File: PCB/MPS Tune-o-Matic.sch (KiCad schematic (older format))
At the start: 19 parts, among them J1 ISP, J2 MPS, U1 ATmega328P, U4 BMP390, Y1 FA-238 16.0000MB-C3

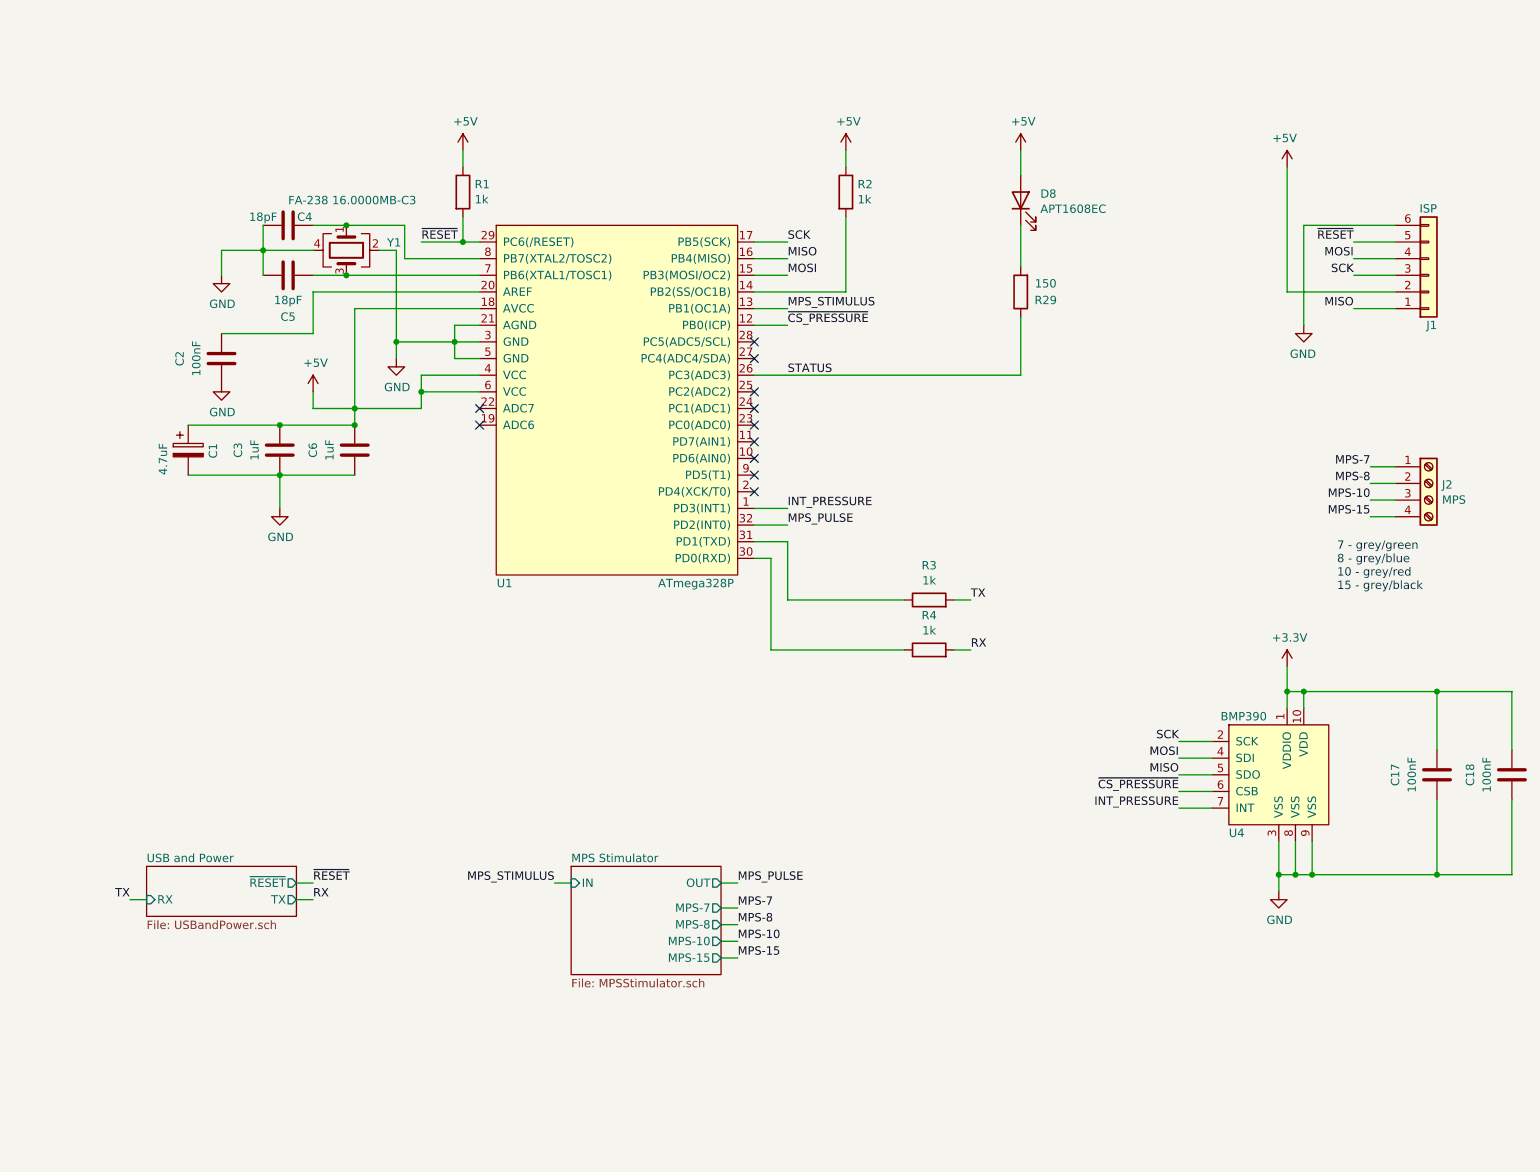
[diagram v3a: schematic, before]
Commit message: Started work on V2.0 with vacuum monitoring.
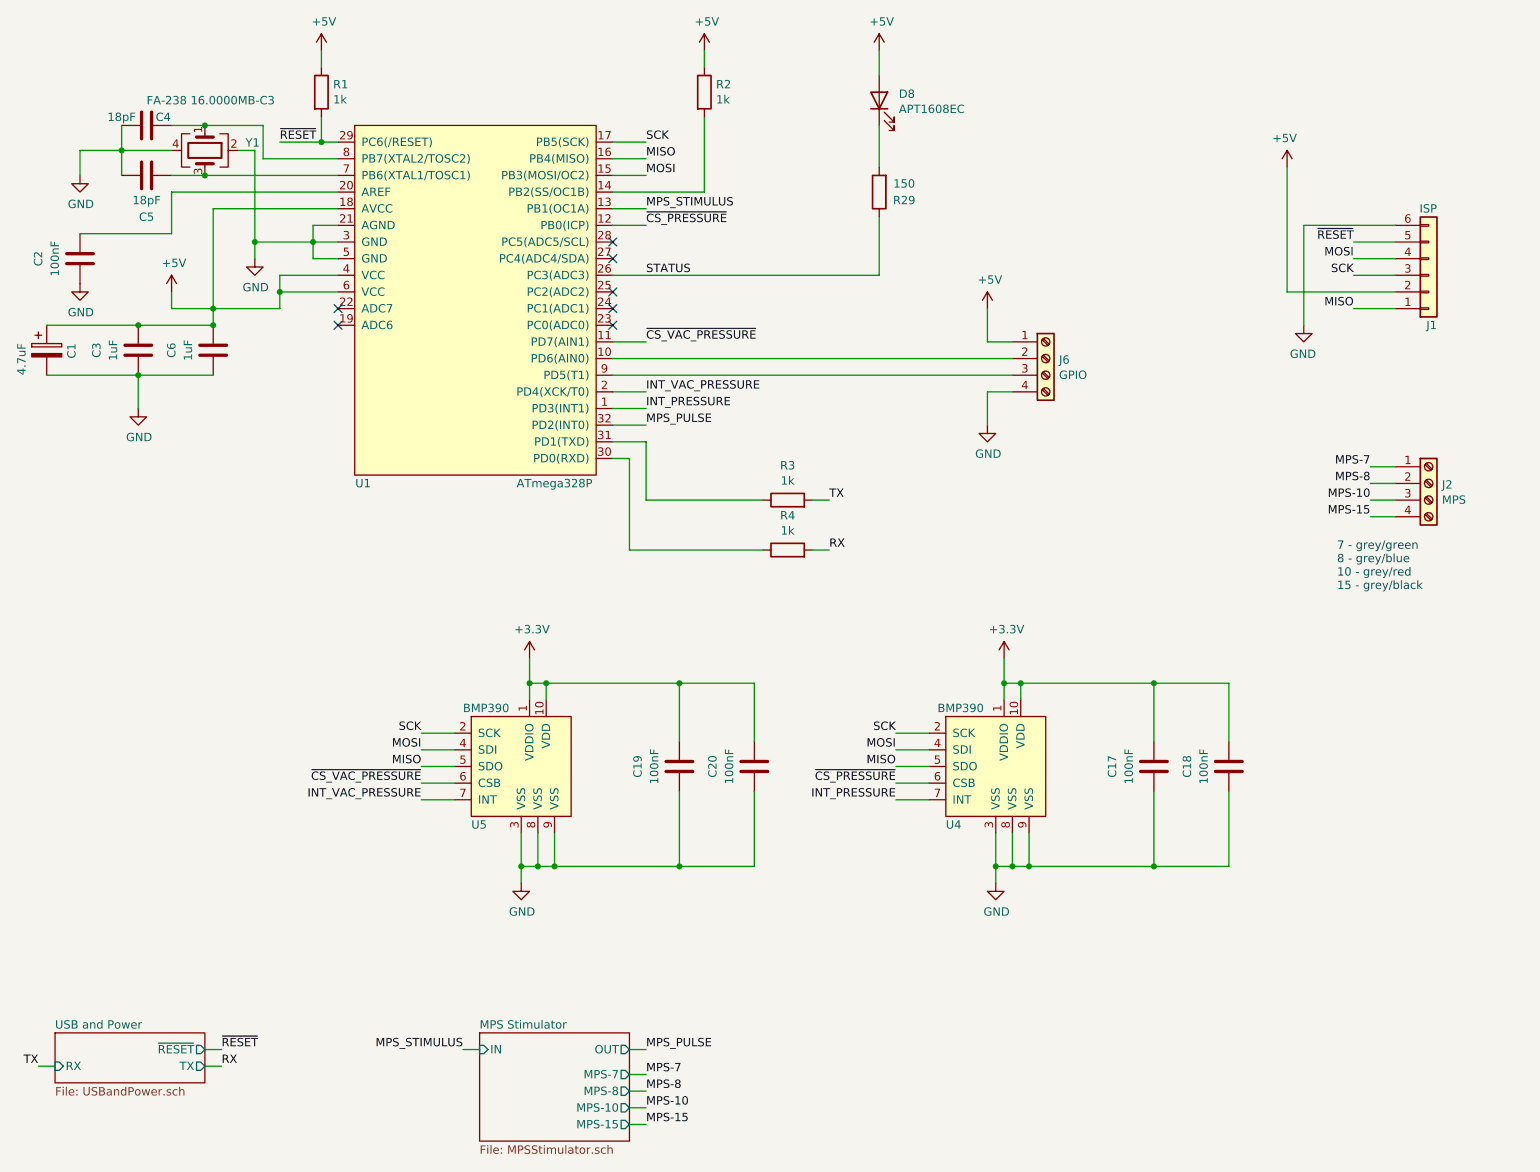
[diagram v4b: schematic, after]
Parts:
- added C19, C20: 100nF, Capacitor_SMD:C_0603_1608Metric, symbol Device:C
- added J6: GPIO, Britishideas:PhoenixContact_COMBICON_PT_4, symbol Connector:Screw_Terminal_01x04
- added U5: BMP390, Britishideas:LGA-2x2-10-pin, symbol BritishIdeas:BMP390
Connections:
- net +3V3: now also C19.1, C20.1, U5.1 (VDDIO), U5.10 (VDD)
- net +5V: now also J6.1 (Pin_1)
- net GND: now also C19.2, C20.2, J6.4 (Pin_4), U5.3 (VSS), U5.8 (VSS), U5.9 (VSS)
- net MISO: now also U5.5 (SDO)
- net MOSI: now also U5.4 (SDI)
- net SCK: now also U5.2 (SCK)
- net at U1.10 (PD6(AIN0)): now also J6.2 (Pin_2)
- net ~CS_VAC_PRESSURE: now reaches U1.11 (PD7(AIN1))
- net ~CS_VAC_PRESSURE: now also U5.6 (CSB)
- net INT_VAC_PRESSURE: now reaches U1.2 (PD4(XCK/T0))
- net INT_VAC_PRESSURE: now also U5.7 (INT)
- net at U1.9 (PD5(T1)): now also J6.3 (Pin_3)
- no-connect marks 11 -> 7
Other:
- moved on the sheet: C1, C17, C18, C2, C3, C4, C5, C6, D8, R1, R2, R29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
